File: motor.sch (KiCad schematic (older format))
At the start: 44 parts, among them J5 70543-0003, Q10 PMPB11EN, Q3 PMPB11EN, Q4 PMPB11EN, Q5 PMPB11EN, Q6 PMPB11EN, Q7 PMPB11EN, Q8 PMPB11EN, Q9 PMPB11EN, U6 TMC2160-TA

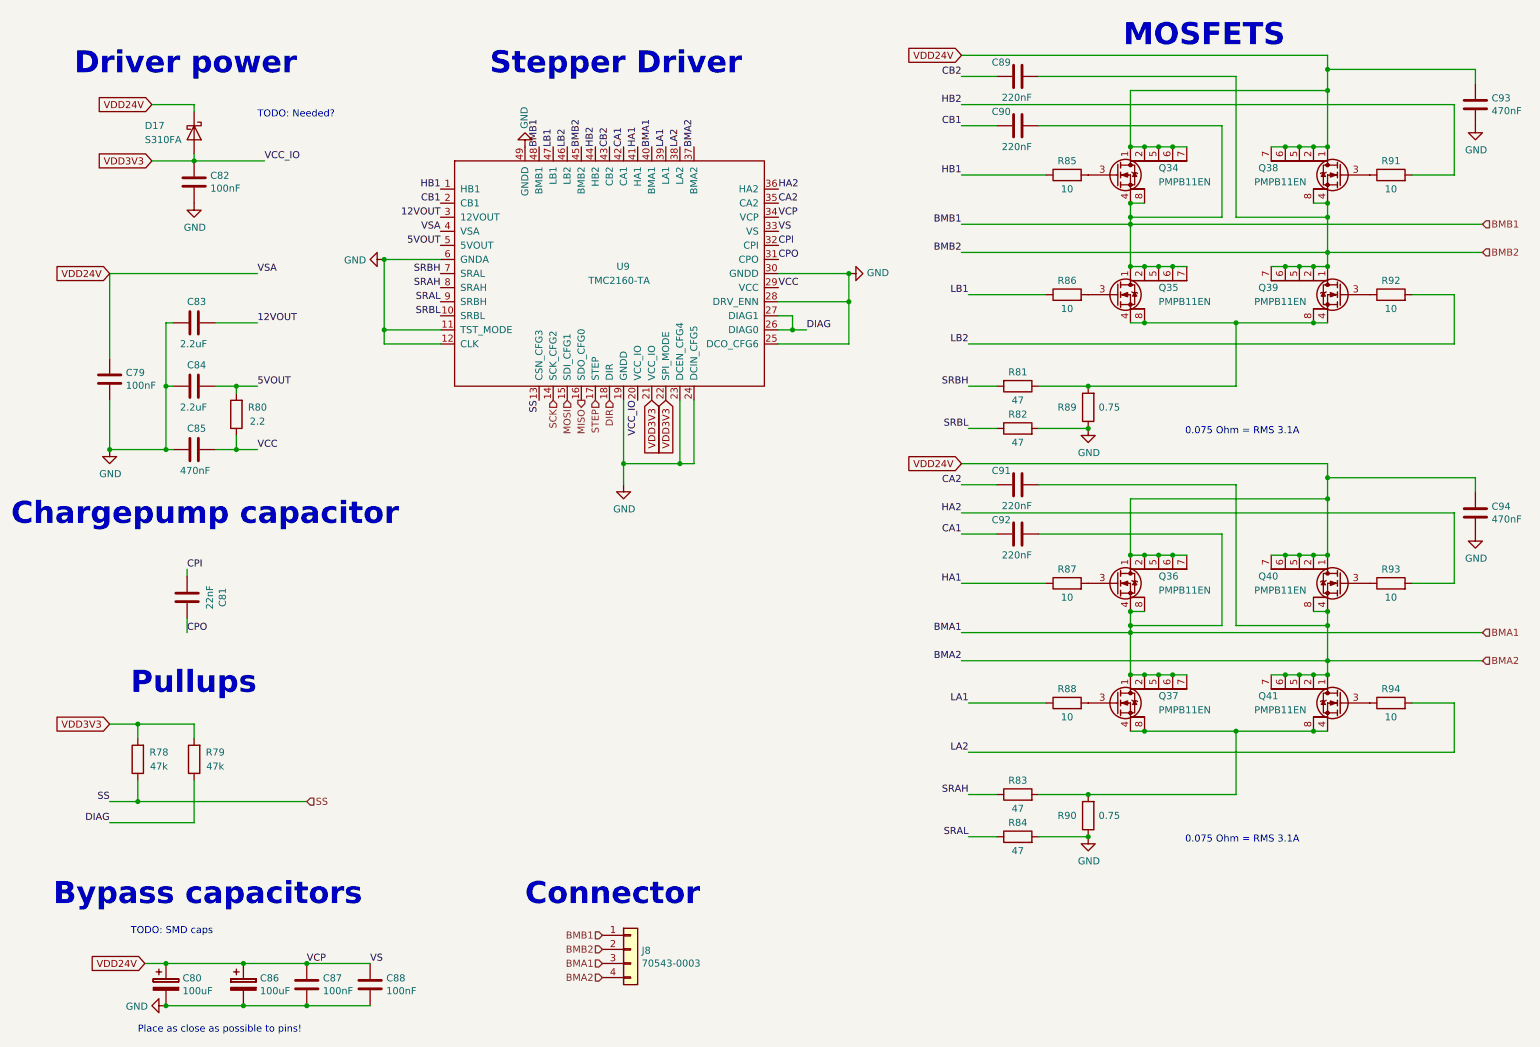
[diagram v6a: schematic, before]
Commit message: Add transistor for boot selection
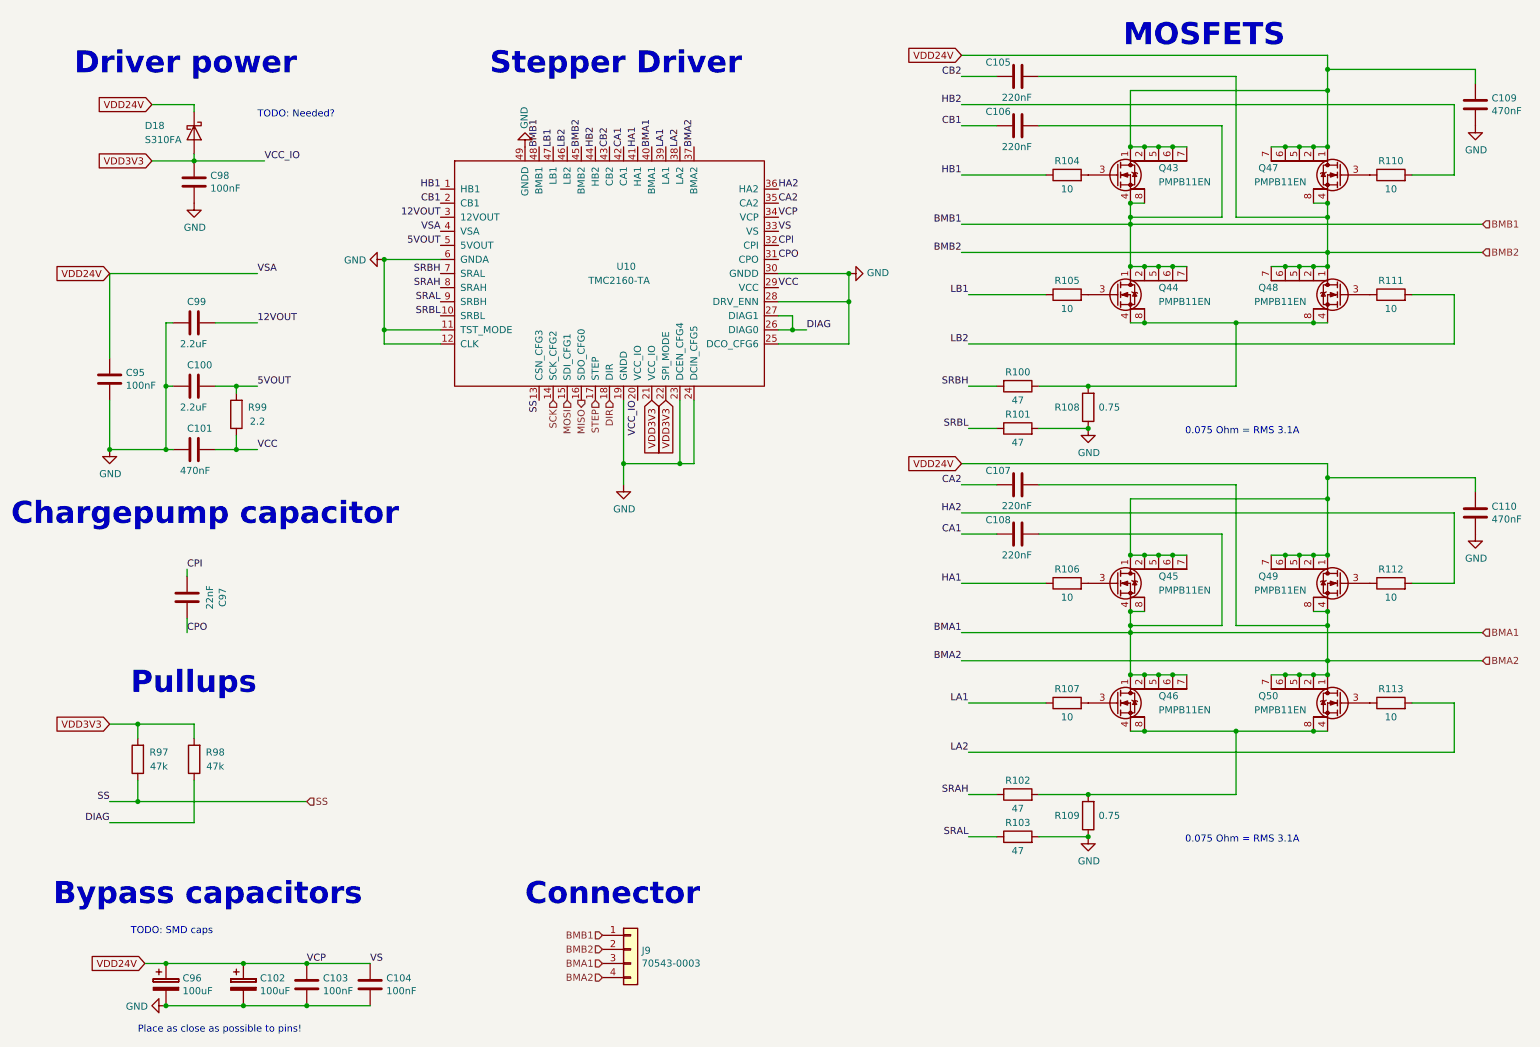
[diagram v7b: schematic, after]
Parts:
- renumbered Q9 to Q10, Q10 to Q11, Q3 to Q4, Q4 to Q5, Q5 to Q6, Q6 to Q7, Q7 to Q8, Q8 to Q9, R13 to R15, R14 to R16, R15 to R17, R16 to R18, R17 to R19, R18 to R20, R19 to R21, R20 to R22, R21 to R23, R22 to R24, R23 to R25, R24 to R26, R25 to R27, R26 to R28, R27 to R29, R28 to R30, R29 to R31

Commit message: Fix current sense resistor to correct value and add BOM
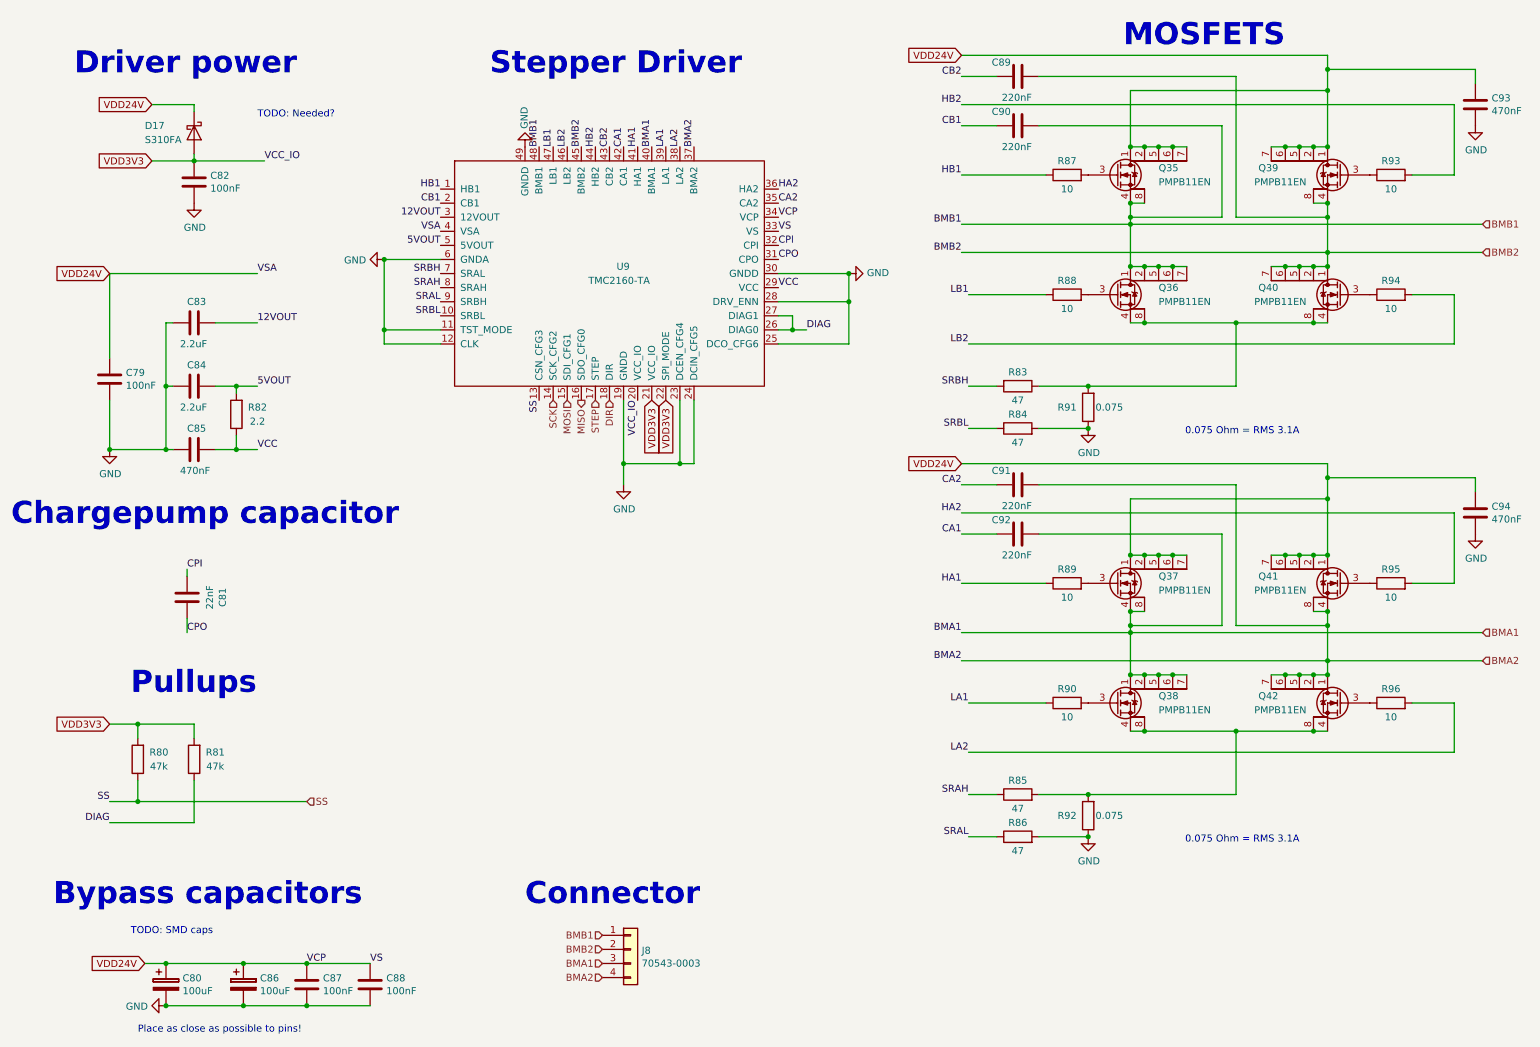
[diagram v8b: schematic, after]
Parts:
- R26, R27: value 0.75 -> 0.075
